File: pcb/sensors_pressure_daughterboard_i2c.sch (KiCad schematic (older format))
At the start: 2 parts

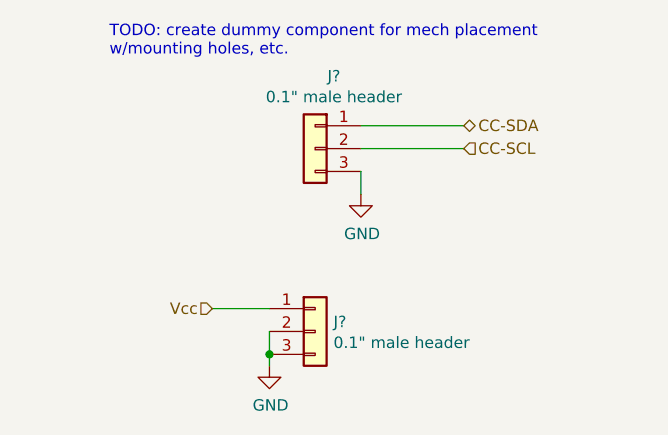
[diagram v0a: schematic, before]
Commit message: Pressure sensor + RTC changes
Added ~enable output to blower connector, changed connector
Misc. adj. to blower ctrl connector to work with all candidate blowers
Replaced discrete level shifter for blower
Added optional PWM filter to blower ctrl for generating analog ctrl voltage
Added mechanical footprints for pressure sensor daughterboards
Linked footprint for RTC's battery holder
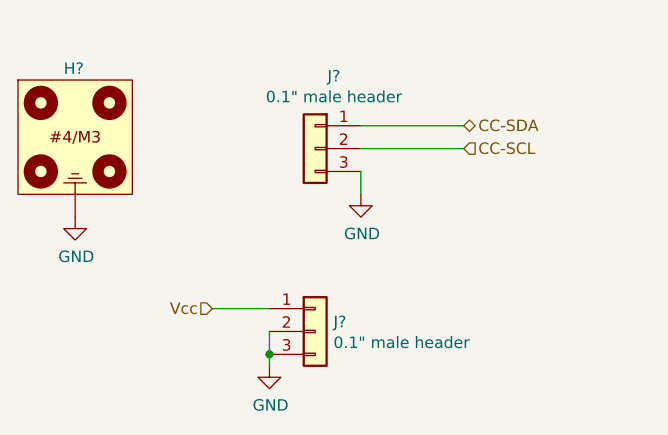
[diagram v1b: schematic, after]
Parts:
- added H?: Pressure_sensor_daughterboard, RespiraWorks:Pressure_sensor_daughterboard, symbol RespiraWorks:Pressure_sensor_daughterboard
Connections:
- net GND: now also H?.1
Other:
- note removed: "TODO: create dummy component for mech placement\nw/mounting holes, etc."
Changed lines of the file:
@@
 $Descr A4 11693 8268
 encoding utf-8
-Sheet 20 30
+Sheet 21 30
 Title "Pressure Sensor Daughterboard Connections, I2C"
 Date ""
@@
 	-1   0    0    -1
 $EndComp
-Text Notes 4400 2950 0    50   ~ 0
-TODO: create dummy component for mech placement\nw/mounting holes, etc.
 $Comp
 L power:GND #PWR?
@@
 Text HLabel 4850 4050 0    50   Input ~ 0
 Vcc
+$Comp
+L RespiraWorks:Pressure_sensor_daughterboard H?
+U 1 1 60542EC5
+P 4250 3550
+F 0 "H?" H 4200 4100 50  0000 L CNN
+F 1 "Pressure_sensor_daughterboard" H 4250 4125 50  0001 C CNN
+F 2 "RespiraWorks:Pressure_sensor_daughterboard" H 4250 3550 50  0001 C CNN
+F 3 "~" H 4250 3550 50  0001 C CNN
+	1    4250 3550
+	1    0    0    -1
+$EndComp
+$Comp
+L power:GND #PWR?
+U 1 1 6054324C
+P 4250 3650
+AR Path="/5FCD4B8E/5FCD4BC5/6054324C" Ref="#PWR?"  Part="1"
+AR Path="/5FCD4B8E/5FE27F70/6054324C" Ref="#PWR?"  Part="1"
+AR Path="/5FCD4D85/6054324C" Ref="#PWR?"  Part="1"
+AR Path="/5FCD4E9D/6054324C" Ref="#PWR?"  Part="1"
+AR Path="/5FCD4E9D/600630A6/6054324C" Ref="#PWR?"  Part="1"
+AR Path="/5FCD4E9D/60073FCF/6054324C" Ref="#PWR?"  Part="1"
+AR Path="/5FCD4E9D/6007AC3B/6054324C" Ref="#PWR?"  Part="1"
+AR Path="/5FCD4E9D/6007BD34/6054324C" Ref="#PWR?"  Part="1"
+AR Path="/5FCD4E9D/6007DA64/6054324C" Ref="#PWR?"  Part="1"
+AR Path="/5FCD4E9D/6007E2BB/6054324C" Ref="#PWR?"  Part="1"
+AR Path="/5FCD4E9D/600CF516/6054324C" Ref="#PWR?"  Part="1"
+AR Path="/5FCD4E9D/600D74A6/6054324C" Ref="#PWR?"  Part="1"
+F 0 "#PWR?" H 4250 3400 50  0001 C CNN
+F 1 "GND" H 4255 3477 50  0000 C CNN
+F 2 "" H 4250 3650 50  0001 C CNN
+F 3 "" H 4250 3650 50  0001 C CNN
+	1    4250 3650
+	1    0    0    -1
+$EndComp
 $EndSCHEMATC
